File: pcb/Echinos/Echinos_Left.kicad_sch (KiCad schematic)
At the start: 0 parts

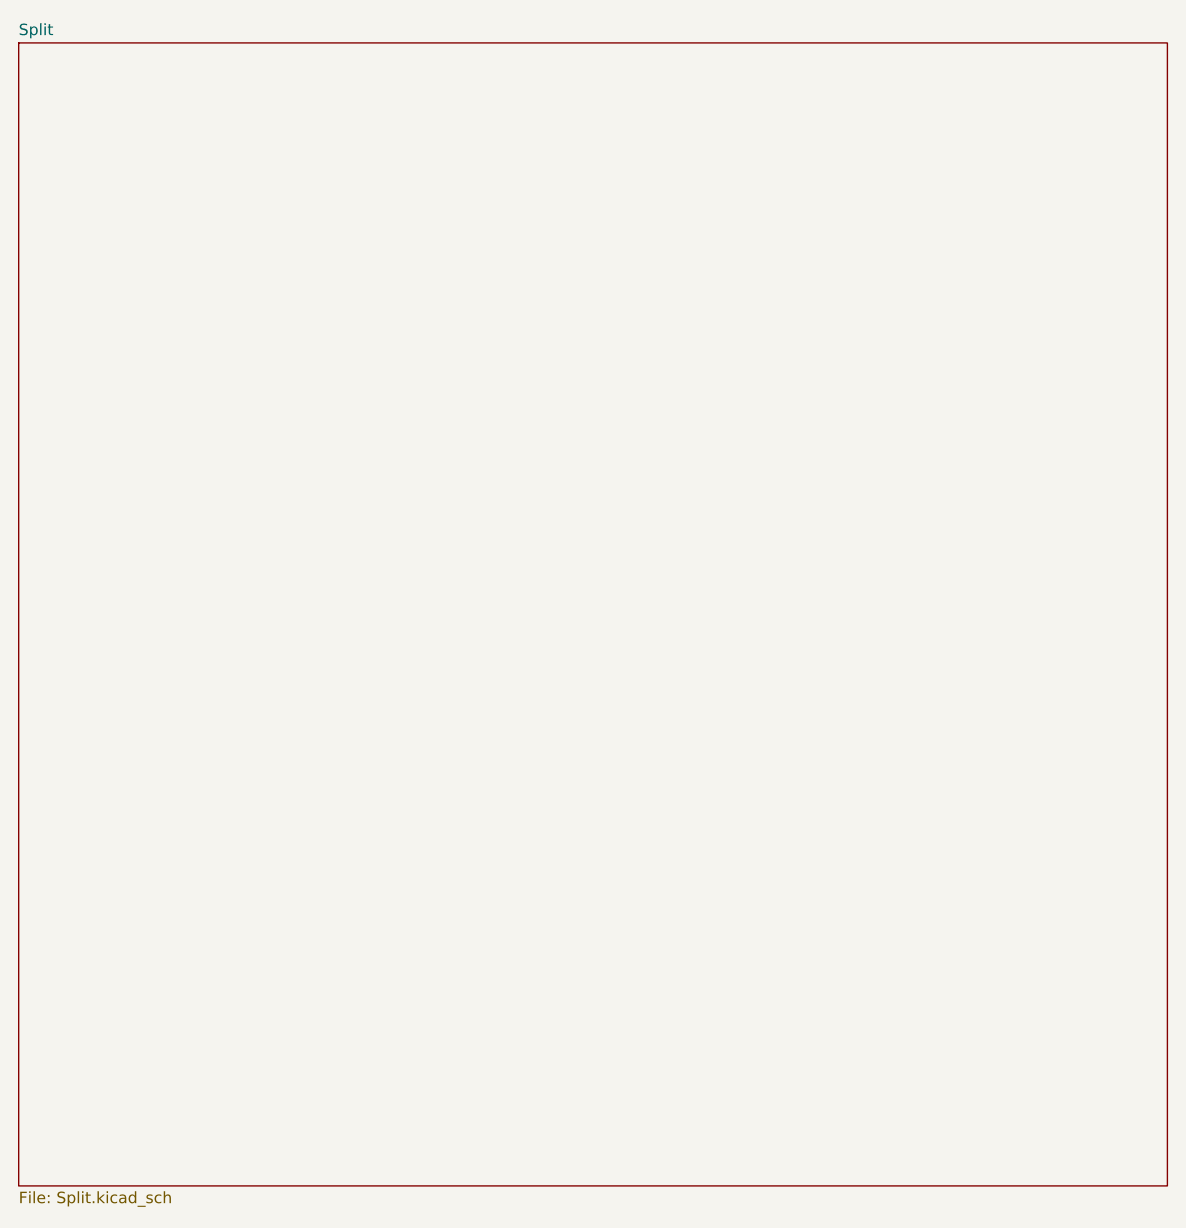
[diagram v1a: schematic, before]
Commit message: 💥 [PCB] - Split schematic for left and right halves.   - Required to create a common PCB to lower the manufacturing cost
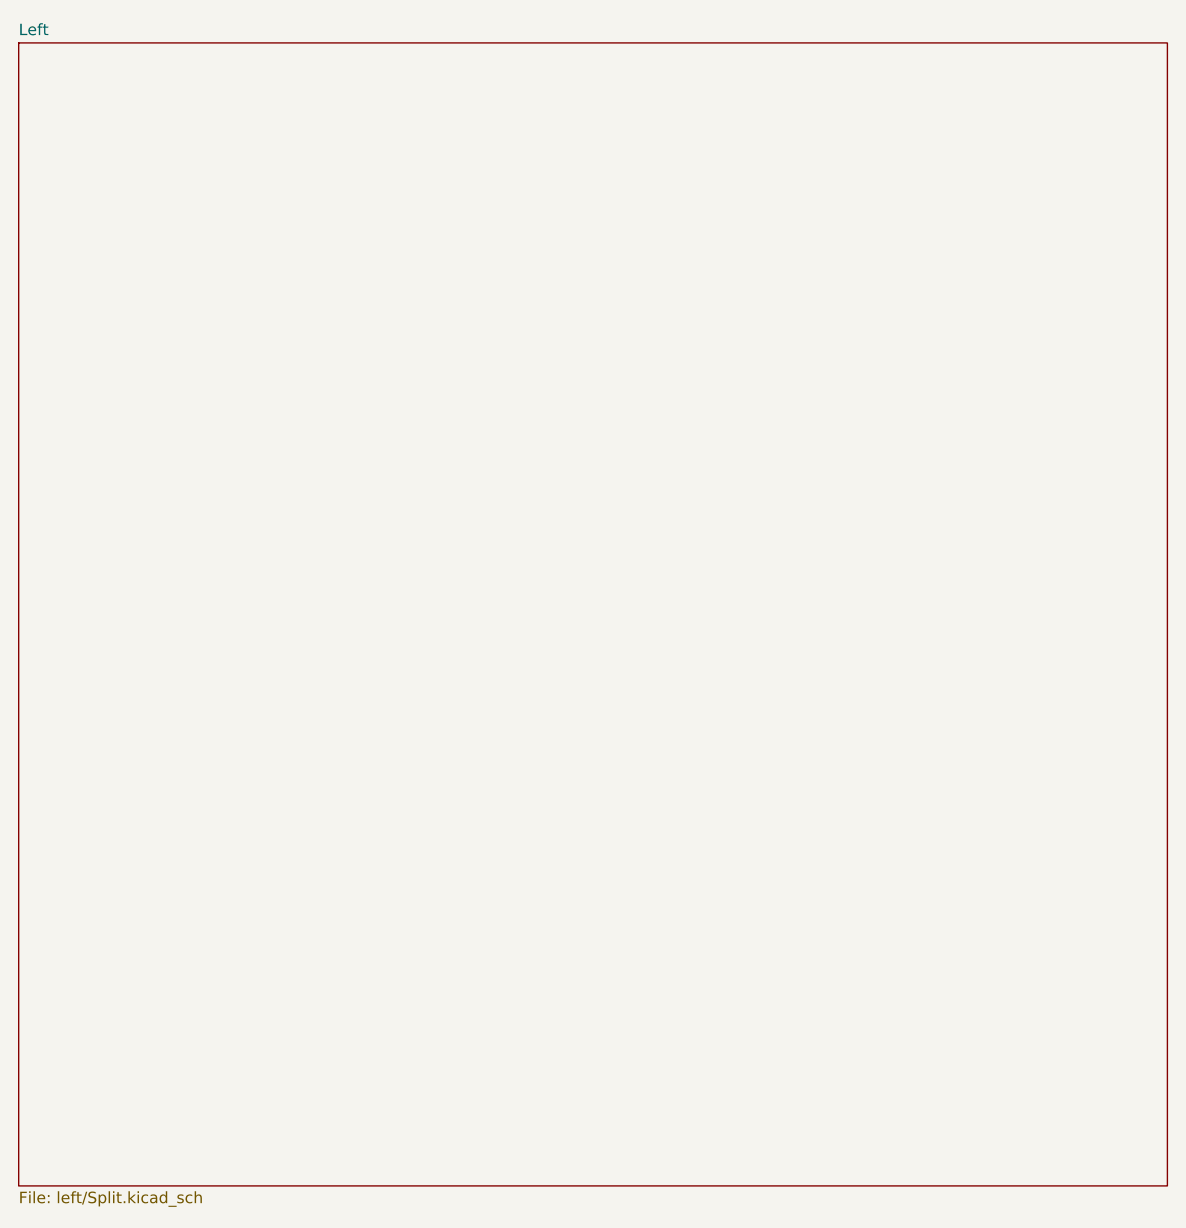
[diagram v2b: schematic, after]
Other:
- sheet Split renamed Left
- sheet Left: file Split.kicad_sch -> left/Split.kicad_sch
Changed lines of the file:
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@@
 			(color 0 0 0 0)
 		)
-		(property "Sheetname" "Split"
+		(property "Sheetname" "Left"
 			(at 63.5 62.1534 0)
 			(show_name no)
@@
 			)
 		)
-		(property "Sheetfile" "Split.kicad_sch"
+		(property "Sheetfile" "left/Split.kicad_sch"
 			(at 63.5 190.4496 0)
 			(show_name no)
